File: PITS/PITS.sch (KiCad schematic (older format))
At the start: 41 parts, among them M2 BME280, P1 CONN_02X20, P14 BATT, P2 BNC, P3 BNC, P4 BNC, P5 BNC, P6 Batt, P7 SENSOR, U1 HX1, U2 MAX-M8C/Q, U3 MTX2, U4 RFM9*, U7 MCP3426

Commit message: Some cleanup
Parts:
- C2: footprint (none) -> Capacitors_SMD:C_0603_HandSoldering
- JP1: footprint (none) -> Resistors_SMD:R_0603_HandSoldering
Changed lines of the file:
@@
 $EndComp
 $Comp
-L +3V3 #PWR12
+L +3V3 #PWR01
 U 1 1 581892DA
 P 4200 3200
-F 0 "#PWR12" H 4200 3050 50  0001 C CNN
+F 0 "#PWR01" H 4200 3050 50  0001 C CNN
 F 1 "+3V3" H 4200 3340 50  0000 C CNN
 F 2 "" H 4200 3200 50  0000 C CNN
@@
 $EndComp
 $Comp
-L +5V #PWR19
+L +5V #PWR02
 U 1 1 5818930B
 P 5300 3200
-F 0 "#PWR19" H 5300 3050 50  0001 C CNN
+F 0 "#PWR02" H 5300 3050 50  0001 C CNN
 F 1 "+5V" H 5300 3340 50  0000 C CNN
 F 2 "" H 5300 3200 50  0000 C CNN
@@
 $EndComp
 $Comp
-L GND #PWR16
+L GND #PWR03
 U 1 1 58189333
 P 5200 5300
-F 0 "#PWR16" H 5200 5050 50  0001 C CNN
+F 0 "#PWR03" H 5200 5050 50  0001 C CNN
 F 1 "GND" H 5200 5150 50  0000 C CNN
 F 2 "" H 5200 5300 50  0000 C CNN
@@
 $EndComp
 $Comp
-L GND #PWR13
+L GND #PWR04
 U 1 1 5818936C
 P 4300 5300
-F 0 "#PWR13" H 4300 5050 50  0001 C CNN
+F 0 "#PWR04" H 4300 5050 50  0001 C CNN
 F 1 "GND" H 4300 5150 50  0000 C CNN
 F 2 "" H 4300 5300 50  0000 C CNN
@@
 $EndComp
 $Comp
-L GND #PWR1
+L GND #PWR05
 U 1 1 58199934
 P 1000 3200
-F 0 "#PWR1" H 1000 2950 50  0001 C CNN
+F 0 "#PWR05" H 1000 2950 50  0001 C CNN
 F 1 "GND" H 1000 3050 50  0000 C CNN
 F 2 "" H 1000 3200 50  0000 C CNN
@@
 $EndComp
 $Comp
-L GND #PWR2
+L GND #PWR06
 U 1 1 581999C7
 P 1000 3600
-F 0 "#PWR2" H 1000 3350 50  0001 C CNN
+F 0 "#PWR06" H 1000 3350 50  0001 C CNN
 F 1 "GND" H 1000 3450 50  0000 C CNN
 F 2 "" H 1000 3600 50  0000 C CNN
@@
 $EndComp
 $Comp
-L GND #PWR3
+L GND #PWR07
 U 1 1 58199A53
 P 1000 4000
-F 0 "#PWR3" H 1000 3750 50  0001 C CNN
+F 0 "#PWR07" H 1000 3750 50  0001 C CNN
 F 1 "GND" H 1000 3850 50  0000 C CNN
 F 2 "" H 1000 4000 50  0000 C CNN
@@
 $EndComp
 $Comp
-L GND #PWR4
+L GND #PWR08
 U 1 1 5819A3C8
 P 1000 4400
-F 0 "#PWR4" H 1000 4150 50  0001 C CNN
+F 0 "#PWR08" H 1000 4150 50  0001 C CNN
 F 1 "GND" H 1000 4250 50  0000 C CNN
 F 2 "" H 1000 4400 50  0000 C CNN
@@
 $EndComp
 $Comp
-L GND #PWR5
+L GND #PWR09
 U 1 1 5819A3CE
 P 1000 4800
-F 0 "#PWR5" H 1000 4550 50  0001 C CNN
+F 0 "#PWR09" H 1000 4550 50  0001 C CNN
 F 1 "GND" H 1000 4650 50  0000 C CNN
 F 2 "" H 1000 4800 50  0000 C CNN
@@
 $EndComp
 $Comp
-L GND #PWR6
+L GND #PWR010
 U 1 1 5819A3D4
 P 1000 5200
-F 0 "#PWR6" H 1000 4950 50  0001 C CNN
+F 0 "#PWR010" H 1000 4950 50  0001 C CNN
 F 1 "GND" H 1000 5050 50  0000 C CNN
 F 2 "" H 1000 5200 50  0000 C CNN
@@
 $EndComp
 $Comp
-L GND #PWR28
+L GND #PWR011
 U 1 1 581A77FE
 P 8800 5200
-F 0 "#PWR28" H 8800 4950 50  0001 C CNN
+F 0 "#PWR011" H 8800 4950 50  0001 C CNN
 F 1 "GND" H 8800 5050 50  0000 C CNN
 F 2 "" H 8800 5200 50  0000 C CNN
@@
 $EndComp
 $Comp
-L GND #PWR22
+L GND #PWR012
 U 1 1 581A780B
 P 8500 3800
-F 0 "#PWR22" H 8500 3550 50  0001 C CNN
+F 0 "#PWR012" H 8500 3550 50  0001 C CNN
 F 1 "GND" H 8500 3650 50  0000 C CNN
 F 2 "" H 8500 3800 50  0000 C CNN
@@
 $EndComp
 $Comp
-L +3V3 #PWR27
+L +3V3 #PWR013
 U 1 1 581A7811
 P 8800 3200
-F 0 "#PWR27" H 8800 3050 50  0001 C CNN
+F 0 "#PWR013" H 8800 3050 50  0001 C CNN
 F 1 "+3V3" H 8800 3340 50  0000 C CNN
 F 2 "" H 8800 3200 50  0000 C CNN
@@
 $EndComp
 $Comp
-L GND #PWR15
+L GND #PWR014
 U 1 1 581B5A31
 P 5000 2500
-F 0 "#PWR15" H 5000 2250 50  0001 C CNN
+F 0 "#PWR014" H 5000 2250 50  0001 C CNN
 F 1 "GND" H 5000 2350 50  0000 C CNN
 F 2 "" H 5000 2500 50  0000 C CNN
@@
 $EndComp
 $Comp
-L +3V3 #PWR25
+L +3V3 #PWR015
 U 1 1 581BA557
 P 8800 1000
-F 0 "#PWR25" H 8800 850 50  0001 C CNN
+F 0 "#PWR015" H 8800 850 50  0001 C CNN
 F 1 "+3V3" H 8800 1140 50  0000 C CNN
 F 2 "" H 8800 1000 50  0000 C CNN
@@
 $EndComp
 $Comp
-L GND #PWR26
+L GND #PWR016
 U 1 1 581BA55D
 P 8800 2400
-F 0 "#PWR26" H 8800 2150 50  0001 C CNN
+F 0 "#PWR016" H 8800 2150 50  0001 C CNN
 F 1 "GND" H 8800 2250 50  0000 C CNN
 F 2 "" H 8800 2400 50  0000 C CNN
@@
 $EndComp
 $Comp
-L +5V #PWR7
+L +5V #PWR017
 U 1 1 581BA581
 P 1900 6000
-F 0 "#PWR7" H 1900 5850 50  0001 C CNN
+F 0 "#PWR017" H 1900 5850 50  0001 C CNN
 F 1 "+5V" H 1900 6140 50  0000 C CNN
 F 2 "" H 1900 6000 50  0000 C CNN
@@
 $EndComp
 $Comp
-L GND #PWR8
+L GND #PWR018
 U 1 1 581BA587
 P 1900 7300
-F 0 "#PWR8" H 1900 7050 50  0001 C CNN
+F 0 "#PWR018" H 1900 7050 50  0001 C CNN
 F 1 "GND" H 1900 7150 50  0000 C CNN
 F 2 "" H 1900 7300 50  0000 C CNN
@@
 $EndComp
 $Comp
-L GND #PWR10
+L GND #PWR019
 U 1 1 581C3D03
 P 2000 2500
-F 0 "#PWR10" H 2000 2250 50  0001 C CNN
+F 0 "#PWR019" H 2000 2250 50  0001 C CNN
 F 1 "GND" H 2000 2350 50  0000 C CNN
 F 2 "" H 2000 2500 50  0000 C CNN
@@
 NoConn ~ 3600 1800
 $Comp
-L +3V3 #PWR9
+L +3V3 #PWR020
 U 1 1 581C44B1
 P 2000 900
-F 0 "#PWR9" H 2000 750 50  0001 C CNN
+F 0 "#PWR020" H 2000 750 50  0001 C CNN
 F 1 "+3V3" H 2000 1040 50  0000 C CNN
 F 2 "" H 2000 900 50  0000 C CNN
@@
 GPIO3(SCL1)
 $Comp
-L +3V3 #PWR14
+L +3V3 #PWR021
 U 1 1 581F044F
 P 5000 900
-F 0 "#PWR14" H 5000 750 50  0001 C CNN
+F 0 "#PWR021" H 5000 750 50  0001 C CNN
 F 1 "+3V3" H 5000 1040 50  0000 C CNN
 F 2 "" H 5000 900 50  0000 C CNN
@@
 $EndComp
 $Comp
-L +3V3 #PWR11
+L +3V3 #PWR022
 U 1 1 581F1873
 P 3800 2000
-F 0 "#PWR11" H 3800 1850 50  0001 C CNN
+F 0 "#PWR022" H 3800 1850 50  0001 C CNN
 F 1 "+3V3" H 3800 2140 50  0000 C CNN
 F 2 "" H 3800 2000 50  0000 C CNN
@@
 $EndComp
 $Comp
-L GND #PWR24
+L GND #PWR023
 U 1 1 581F2BC2
 P 8500 6500
-F 0 "#PWR24" H 8500 6250 50  0001 C CNN
+F 0 "#PWR023" H 8500 6250 50  0001 C CNN
 F 1 "GND" H 8500 6350 50  0000 C CNN
 F 2 "" H 8500 6500 50  0000 C CNN
@@
 $EndComp
 $Comp
-L GND #PWR21
+L GND #PWR024
 U 1 1 585C2217
 P 6300 6400
-F 0 "#PWR21" H 6300 6150 50  0001 C CNN
+F 0 "#PWR024" H 6300 6150 50  0001 C CNN
 F 1 "GND" H 6300 6250 50  0000 C CNN
 F 2 "" H 6300 6400 50  0000 C CNN
@@
 $EndComp
 $Comp
-L +3V3 #PWR20
+L +3V3 #PWR025
 U 1 1 585C22B5
 P 6300 6000
-F 0 "#PWR20" H 6300 5850 50  0001 C CNN
+F 0 "#PWR025" H 6300 5850 50  0001 C CNN
 F 1 "+3V3" H 6300 6140 50  0000 C CNN
 F 2 "" H 6300 6000 50  0000 C CNN
@@
 D6
 $Comp
-L +5V_PSU #PWR23
+L +5V_PSU #PWR026
 U 1 1 5990B289
 P 8500 6000
-F 0 "#PWR23" H 8500 5850 50  0001 C CNN
+F 0 "#PWR026" H 8500 5850 50  0001 C CNN
 F 1 "+5V_PSU" H 8500 6140 50  0000 C CNN
 F 2 "" H 8500 6000 50  0000 C CNN
@@
 $EndComp
 $Comp
-L GND #PWR18
+L GND #PWR027
 U 1 1 59A1CFE9
 P 5200 7100
-F 0 "#PWR18" H 5200 6850 50  0001 C CNN
+F 0 "#PWR027" H 5200 6850 50  0001 C CNN
 F 1 "GND" H 5200 6950 50  0000 C CNN
 F 2 "" H 5200 7100 50  0000 C CNN
@@
 $EndComp
 $Comp
-L +3V3 #PWR17
+L +3V3 #PWR028
 U 1 1 59A1CE9E
 P 5200 6000
-F 0 "#PWR17" H 5200 5850 50  0001 C CNN
+F 0 "#PWR028" H 5200 5850 50  0001 C CNN
 F 1 "+3V3" H 5200 6140 50  0000 C CNN
 F 2 "" H 5200 6000 50  0000 C CNN
@@
 F 0 "C2" H 7525 4950 50  0000 L CNN
 F 1 "100n" H 7525 4750 50  0000 L CNN
-F 2 "" H 7538 4700 50  0000 C CNN
+F 2 "Capacitors_SMD:C_0603_HandSoldering" H 7538 4700 50  0001 C CNN
 F 3 "" H 7500 4850 50  0000 C CNN
 	1    7500 4850
@@
 F 0 "JP1" H 8400 5180 50  0000 C CNN
 F 1 "CH2- to GND" H 8410 5040 50  0000 C CNN
-F 2 "" H 8400 5100 50  0000 C CNN
+F 2 "Resistors_SMD:R_0603_HandSoldering" H 8400 5100 50  0001 C CNN
 F 3 "" H 8400 5100 50  0000 C CNN
 	1    8400 5100

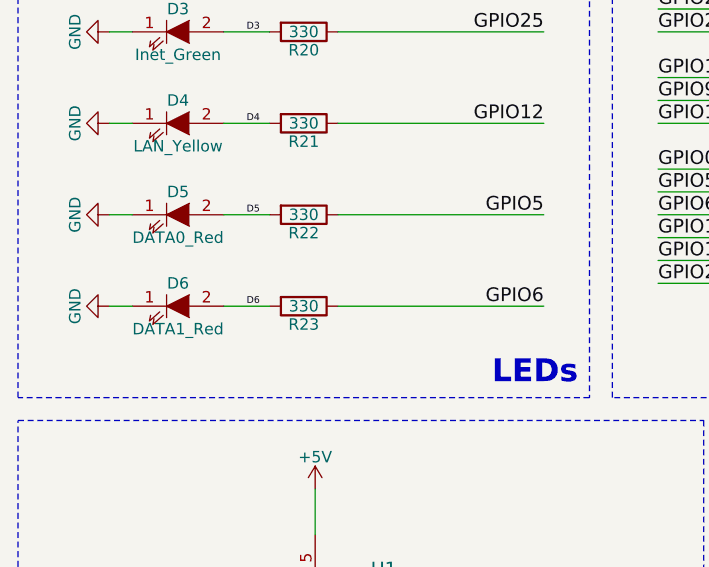
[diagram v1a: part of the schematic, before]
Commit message: removed scound LORA led
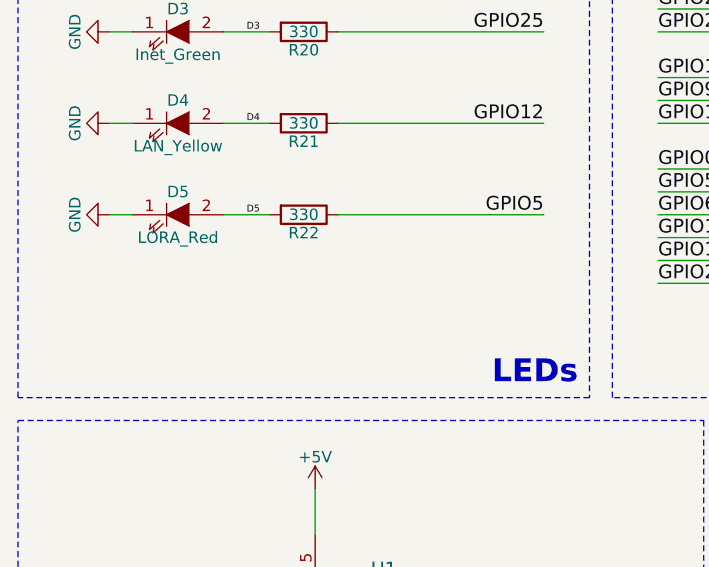
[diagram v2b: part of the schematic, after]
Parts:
- removed D6: DATA1_Red, LEDs:LED_0603, symbol LED
- removed R23: 330, Resistors_SMD:R_0603_HandSoldering, symbol R
- D5: value DATA0_Red -> LORA_Red
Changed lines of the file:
@@
 P 1300 4800
 F 0 "D5" H 1300 4900 50  0000 C CNN
-F 1 "DATA0_Red" H 1300 4700 50  0000 C CNN
+F 1 "LORA_Red" H 1300 4700 50  0000 C CNN
 F 2 "LEDs:LED_0603" H 1300 4800 50  0001 C CNN
 F 3 "" H 1300 4800 50  0000 C CNN
 	1    1300 4800
-	1    0    0    -1
-$EndComp
-$Comp
-L LED D6
-U 1 1 5819A3A9
-P 1300 5200
-F 0 "D6" H 1300 5300 50  0000 C CNN
-F 1 "DATA1_Red" H 1300 5100 50  0000 C CNN
-F 2 "LEDs:LED_0603" H 1300 5200 50  0001 C CNN
-F 3 "" H 1300 5200 50  0000 C CNN
-	1    1300 5200
 	1    0    0    -1
 $EndComp
@@
 $EndComp
 $Comp
-L R R23
-U 1 1 5819A3BE
-P 1850 5200
-F 0 "R23" V 1930 5200 50  0000 C CNN
-F 1 "330" V 1850 5200 50  0000 C CNN
-F 2 "Resistors_SMD:R_0603_HandSoldering" V 1780 5200 50  0001 C CNN
-F 3 "" H 1850 5200 50  0000 C CNN
-	1    1850 5200
-	0    1    1    0
-$EndComp
-$Comp
 L GND #PWR08
 U 1 1 5819A3C8
@@
 F 3 "" H 1000 4800 50  0000 C CNN
 	1    1000 4800
-	0    1    1    0
-$EndComp
-$Comp
-L GND #PWR010
-U 1 1 5819A3D4
-P 1000 5200
-F 0 "#PWR010" H 1000 4950 50  0001 C CNN
-F 1 "GND" H 1000 5050 50  0000 C CNN
-F 2 "" H 1000 5200 50  0000 C CNN
-F 3 "" H 1000 5200 50  0000 C CNN
-	1    1000 5200
 	0    1    1    0
 $EndComp
@@
 Text Label 1600 4800 0    30   ~ 0
 D5
-Text Label 1600 5200 0    30   ~ 0
-D6
 $Comp
 L +5V_PSU #PWR026
@@
 Text Label 2900 4800 2    60   ~ 0
 GPIO5
-Text Label 2900 5200 2    60   ~ 0
-GPIO6
 Text Label 2900 4400 2    60   ~ 0
 GPIO12
@@
 	8800 5200 8800 5000
 Wire Wire Line
-	2000 5200 2900 5200
-Wire Wire Line
 	2000 4800 2900 4800
 Wire Wire Line
@@
 	2000 3200 2900 3200
 Wire Wire Line
-	1000 5200 1100 5200
-Wire Wire Line
 	1000 4800 1100 4800
 Wire Wire Line
 	1000 4400 1100 4400
 Wire Wire Line
-	1500 5200 1700 5200
-Wire Wire Line
 	1700 4800 1500 4800

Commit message: PCB save
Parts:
- P7: footprint Connectors:SMD_5_xsmall -> Pin_Headers:Pin_Header_Straight_1x05_Pitch2.54mm
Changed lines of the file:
@@
 $EndComp
 $Comp
-L GND #PWR011
+L GND #PWR010
 U 1 1 581A77FE
 P 8800 5200
-F 0 "#PWR011" H 8800 4950 50  0001 C CNN
+F 0 "#PWR010" H 8800 4950 50  0001 C CNN
 F 1 "GND" H 8800 5050 50  0000 C CNN
 F 2 "" H 8800 5200 50  0000 C CNN
@@
 $EndComp
 $Comp
-L GND #PWR012
+L GND #PWR011
 U 1 1 581A780B
 P 8500 3800
-F 0 "#PWR012" H 8500 3550 50  0001 C CNN
+F 0 "#PWR011" H 8500 3550 50  0001 C CNN
 F 1 "GND" H 8500 3650 50  0000 C CNN
 F 2 "" H 8500 3800 50  0000 C CNN
@@
 $EndComp
 $Comp
-L +3V3 #PWR013
+L +3V3 #PWR012
 U 1 1 581A7811
 P 8800 3200
-F 0 "#PWR013" H 8800 3050 50  0001 C CNN
+F 0 "#PWR012" H 8800 3050 50  0001 C CNN
 F 1 "+3V3" H 8800 3340 50  0000 C CNN
 F 2 "" H 8800 3200 50  0000 C CNN
@@
 $EndComp
 $Comp
-L GND #PWR014
+L GND #PWR013
 U 1 1 581B5A31
 P 5000 2500
-F 0 "#PWR014" H 5000 2250 50  0001 C CNN
+F 0 "#PWR013" H 5000 2250 50  0001 C CNN
 F 1 "GND" H 5000 2350 50  0000 C CNN
 F 2 "" H 5000 2500 50  0000 C CNN
@@
 $EndComp
 $Comp
-L +3V3 #PWR015
+L +3V3 #PWR014
 U 1 1 581BA557
 P 8800 1000
-F 0 "#PWR015" H 8800 850 50  0001 C CNN
+F 0 "#PWR014" H 8800 850 50  0001 C CNN
 F 1 "+3V3" H 8800 1140 50  0000 C CNN
 F 2 "" H 8800 1000 50  0000 C CNN
@@
 $EndComp
 $Comp
-L GND #PWR016
+L GND #PWR015
 U 1 1 581BA55D
 P 8800 2400
-F 0 "#PWR016" H 8800 2150 50  0001 C CNN
+F 0 "#PWR015" H 8800 2150 50  0001 C CNN
 F 1 "GND" H 8800 2250 50  0000 C CNN
 F 2 "" H 8800 2400 50  0000 C CNN
@@
 $EndComp
 $Comp
-L +5V #PWR017
+L +5V #PWR016
 U 1 1 581BA581
 P 1900 6000
-F 0 "#PWR017" H 1900 5850 50  0001 C CNN
+F 0 "#PWR016" H 1900 5850 50  0001 C CNN
 F 1 "+5V" H 1900 6140 50  0000 C CNN
 F 2 "" H 1900 6000 50  0000 C CNN
@@
 $EndComp
 $Comp
-L GND #PWR018
+L GND #PWR017
 U 1 1 581BA587
 P 1900 7300
-F 0 "#PWR018" H 1900 7050 50  0001 C CNN
+F 0 "#PWR017" H 1900 7050 50  0001 C CNN
 F 1 "GND" H 1900 7150 50  0000 C CNN
 F 2 "" H 1900 7300 50  0000 C CNN
@@
 $EndComp
 $Comp
-L GND #PWR019
+L GND #PWR018
 U 1 1 581C3D03
 P 2000 2500
-F 0 "#PWR019" H 2000 2250 50  0001 C CNN
+F 0 "#PWR018" H 2000 2250 50  0001 C CNN
 F 1 "GND" H 2000 2350 50  0000 C CNN
 F 2 "" H 2000 2500 50  0000 C CNN
@@
 NoConn ~ 3600 1800
 $Comp
-L +3V3 #PWR020
+L +3V3 #PWR019
 U 1 1 581C44B1
 P 2000 900
-F 0 "#PWR020" H 2000 750 50  0001 C CNN
+F 0 "#PWR019" H 2000 750 50  0001 C CNN
 F 1 "+3V3" H 2000 1040 50  0000 C CNN
 F 2 "" H 2000 900 50  0000 C CNN
@@
 GPIO3(SCL1)
 $Comp
-L +3V3 #PWR021
+L +3V3 #PWR020
 U 1 1 581F044F
 P 5000 900
-F 0 "#PWR021" H 5000 750 50  0001 C CNN
+F 0 "#PWR020" H 5000 750 50  0001 C CNN
 F 1 "+3V3" H 5000 1040 50  0000 C CNN
 F 2 "" H 5000 900 50  0000 C CNN
@@
 $EndComp
 $Comp
-L +3V3 #PWR022
+L +3V3 #PWR021
 U 1 1 581F1873
 P 3800 2000
-F 0 "#PWR022" H 3800 1850 50  0001 C CNN
+F 0 "#PWR021" H 3800 1850 50  0001 C CNN
 F 1 "+3V3" H 3800 2140 50  0000 C CNN
 F 2 "" H 3800 2000 50  0000 C CNN
@@
 $EndComp
 $Comp
-L GND #PWR023
+L GND #PWR022
 U 1 1 581F2BC2
 P 8500 6500
-F 0 "#PWR023" H 8500 6250 50  0001 C CNN
+F 0 "#PWR022" H 8500 6250 50  0001 C CNN
 F 1 "GND" H 8500 6350 50  0000 C CNN
 F 2 "" H 8500 6500 50  0000 C CNN
@@
 $EndComp
 $Comp
-L GND #PWR024
+L GND #PWR023
 U 1 1 585C2217
 P 6300 6400
-F 0 "#PWR024" H 6300 6150 50  0001 C CNN
+F 0 "#PWR023" H 6300 6150 50  0001 C CNN
 F 1 "GND" H 6300 6250 50  0000 C CNN
 F 2 "" H 6300 6400 50  0000 C CNN
@@
 $EndComp
 $Comp
-L +3V3 #PWR025
+L +3V3 #PWR024
 U 1 1 585C22B5
 P 6300 6000
-F 0 "#PWR025" H 6300 5850 50  0001 C CNN
+F 0 "#PWR024" H 6300 5850 50  0001 C CNN
 F 1 "+3V3" H 6300 6140 50  0000 C CNN
 F 2 "" H 6300 6000 50  0000 C CNN
@@
 D5
 $Comp
-L +5V_PSU #PWR026
+L +5V_PSU #PWR025
 U 1 1 5990B289
 P 8500 6000
-F 0 "#PWR026" H 8500 5850 50  0001 C CNN
+F 0 "#PWR025" H 8500 5850 50  0001 C CNN
 F 1 "+5V_PSU" H 8500 6140 50  0000 C CNN
 F 2 "" H 8500 6000 50  0000 C CNN
@@
 F 0 "P7" H 5600 7000 50  0000 C CNN
 F 1 "SENSOR" V 5700 6700 50  0000 C CNN
-F 2 "Connectors:SMD_5_xsmall" H 5600 6700 50  0001 C CNN
+F 2 "Pin_Headers:Pin_Header_Straight_1x05_Pitch2.54mm" H 5600 6700 50  0001 C CNN
 F 3 "" H 5600 6700 50  0000 C CNN
 	1    5600 6700
@@
 $EndComp
 $Comp
-L GND #PWR027
+L GND #PWR026
 U 1 1 59A1CFE9
 P 5200 7100
-F 0 "#PWR027" H 5200 6850 50  0001 C CNN
+F 0 "#PWR026" H 5200 6850 50  0001 C CNN
 F 1 "GND" H 5200 6950 50  0000 C CNN
 F 2 "" H 5200 7100 50  0000 C CNN
@@
 $EndComp
 $Comp
-L +3V3 #PWR028
+L +3V3 #PWR027
 U 1 1 59A1CE9E
 P 5200 6000
-F 0 "#PWR028" H 5200 5850 50  0001 C CNN
+F 0 "#PWR027" H 5200 5850 50  0001 C CNN
 F 1 "+3V3" H 5200 6140 50  0000 C CNN
 F 2 "" H 5200 6000 50  0000 C CNN

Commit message: all power routing done
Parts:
- P14, P6: footprint Pin_Headers:Pin_Header_Straight_1x02_Pitch2.00mm -> Connectors:SMD_2_xsmall
- P7: footprint Pin_Headers:Pin_Header_Straight_1x05_Pitch2.54mm -> Connectors:SMD_5_xsmall
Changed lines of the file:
@@
 F 0 "P14" H 8900 6400 50  0000 C CNN
 F 1 "BATT" V 9000 6250 50  0000 C CNN
-F 2 "Pin_Headers:Pin_Header_Straight_1x02_Pitch2.00mm" H 8900 6250 50  0001 C CNN
+F 2 "Connectors:SMD_2_xsmall" H 8900 6250 50  0001 C CNN
 F 3 "" H 8900 6250 50  0000 C CNN
 	1    8900 6250
@@
 F 0 "P7" H 5600 7000 50  0000 C CNN
 F 1 "SENSOR" V 5700 6700 50  0000 C CNN
-F 2 "Pin_Headers:Pin_Header_Straight_1x05_Pitch2.54mm" H 5600 6700 50  0001 C CNN
+F 2 "Connectors:SMD_5_xsmall" H 5600 6700 50  0001 C CNN
 F 3 "" H 5600 6700 50  0000 C CNN
 	1    5600 6700
@@
 F 0 "P6" H 6700 5200 50  0000 C CNN
 F 1 "Batt" V 6800 5050 50  0000 C CNN
-F 2 "Pin_Headers:Pin_Header_Straight_1x02_Pitch2.00mm" H 6700 5050 50  0001 C CNN
+F 2 "Connectors:SMD_2_xsmall" H 6700 5050 50  0001 C CNN
 F 3 "" H 6700 5050 50  0000 C CNN
 	1    6700 5050

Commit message: all routing finished!
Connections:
- net GPIO6: now also U3.4 (EN/PGM)
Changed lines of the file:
@@
 	8500 5100 8800 5100
 Connection ~ 8800 5100
+Text Label 10900 1600 2    60   ~ 0
+GPIO6
 $EndSCHEMATC
